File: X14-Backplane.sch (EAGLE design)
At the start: 28 parts, among them J2 PXC-PTSM-04-RA-1778641, J3 PXC-8-RA-1778683, J7 POE_TERMINAL

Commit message: X14-Backplane 11/29
This is the most up to date backplane as of 11/29/2021
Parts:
- removed C5: 47uF, Panasonic 47 uF cap - EEE-1CA470SP:47UF-POLAR-PANASONIC_D-35V-20%
- removed J7: POE_TERMINAL, Dist_POE:POE_TERMINAL
- added J8: PXC-8-RA-1778683, Phoenix Contact PTSM 8 pin:PXC-8-RA-1778683
- added U$9: IPL_13X2, PI-SHIELD, Solenoid-Backplane:IPL_13X2
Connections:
- new net +3V3: U$9.26
- new net ALERT1: U$9.16
- new net ALERT2: U$9.18
- new net SOL1_1: J8.8, U$9.5
- new net SOL2_1: J8.7, U$9.7
- new net SOL3_1: J8.6, U$9.9
- new net SOL4_1: J8.5, U$9.11
- new net SOL5_1: J8.4, U$9.13
- new net SOL6_1: J8.3, U$9.15
- new net SWCLK: U$9.10
- new net SWDIO: U$9.12
- net 12V: now also J8.1, J8.2, U$4.12V, U$9.25; no longer C5.+
- net 5V: now also U$9.2; no longer J7.1
- net C2_1: now also U$9.20
- net C2_2: now also U$9.19
- net CAN_H: now also U$9.21
- net CAN_L: now also U$9.23
- net CLK: now also U$9.22
- net DATA: now also U$9.24
- net GND: now also U$9.1, U$9.14, U$9.17, U$9.3, U$9.4, U$9.6, U$9.8; no longer C5.-, J7.2
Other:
- note added: "CAN io"
- note added: "PI Shield Connector"
- note added: "Power to ESC adapters"
- note added: "Reset Diode"
- note added: "Solenoid"
- note removed: "Prob dont need - note to ask grant"

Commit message: X14-Backplane 12/2
Most up to date backplane as of 12/2/2021
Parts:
- U$9: value IPL_13X2 -> 6X_CONN; device PI-SHIELD, Solenoid-Backplane:IPL_13X2 -> PI-SHIELD, Solenoid-Backplane:6X_CONN
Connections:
- removed net +3V3: U$9.26
- removed net ALERT1: U$9.16
- removed net ALERT2: U$9.18
- removed net GND: C4.2, J2.1, J3.1, J6.4, MUX.GND, MUX.GND2, MUX.INH, R1.1, R4.1, R5.1, U$1.10, U$2.10, U$3.10, U$4.GND_5V, U$8.P$1, U$9.1, U$9.14, U$9.17, U$9.3, U$9.4, U$9.6, U$9.8
- removed net SWCLK: U$9.10
- removed net SWDIO: U$9.12
- new net 12V_L: J8.1, J8.2, U$4.12V, U$9.14, U$9.16
- new net GND_L: C4.2, J2.1, J3.1, J6.4, MUX.GND, MUX.GND2, MUX.INH, R1.1, R4.1, R5.1, U$1.10, U$2.10, U$3.10, U$4.GND_12V, U$8.P$1, U$9.18, U$9.22
- new net JH: U$4.GND_5V
- net 12V: no longer J8.1, J8.2, U$4.12V, U$9.25
- net 3V3: now also U$9.24
- net 5V: now also U$9.20; no longer U$9.2
- net C2_1: no longer U$9.20
- net C2_2: no longer U$9.19
- net CAN_H: no longer U$9.21
- net CAN_L: no longer U$9.23
- net CLK: no longer U$9.22
- net DATA: no longer U$9.24
- net SOL1_1: now also J8.3, U$9.13; no longer J8.8, U$9.5
- net SOL2_1: now also J8.4, U$9.15; no longer J8.7, U$9.7
- net SOL3_1: now also J8.5, U$9.17; no longer J8.6, U$9.9
- net SOL4_1: now also J8.6, U$9.19; no longer J8.5, U$9.11
- net SOL5_1: now also J8.7, U$9.21; no longer J8.4, U$9.13
- net SOL6_1: now also J8.8, U$9.23; no longer J8.3, U$9.15

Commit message: X14-Backplane 12/4
This is the most up to date version as of 12/4/2021
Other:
- moved on the sheet: C4, J2, J6, R7, R8

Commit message: routing
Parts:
- removed J6: (no value), te 3.5m mm horiz 4 pin:284512-4
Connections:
- net 5V: no longer J6.1
- net CAN_H: no longer J6.2
- net CAN_L: no longer J6.3
- net GND_L: no longer J6.4
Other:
- note removed: "CAN to Logic"
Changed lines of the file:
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@@
 <part name="R5" library="SparkFun-Resistors" library_urn="urn:adsk.eagle:library:532" deviceset="1KOHM" device="-0603-1/10W-1%" package3d_urn="urn:adsk.eagle:package:39650/1" value="4.7k"/>
 <part name="DIST_TO_BACKPLANE" library="Samtec MPPT Hermaphoditic 10 pos - MPPT-10-01-01-L-RA-SD" deviceset="MPPT-10-01-01-L-RA-SD" device="" package3d_urn="urn:adsk.eagle:package:25115828/2"/>
-<part name="J6" library="te 3.5m mm horiz 4 pin" deviceset="284512-4" device="" package3d_urn="urn:adsk.eagle:package:24291286/2"/>
 <part name="H1" library="Mounting Holes" deviceset="6-32-HOLE" device="" package3d_urn="urn:adsk.eagle:package:24384748/2"/>
 <part name="H2" library="Mounting Holes" deviceset="6-32-HOLE" device="" package3d_urn="urn:adsk.eagle:package:24384748/2"/>
@@
 <sheet>
 <plain>
-<text x="149.86" y="-46.99" size="1.778" layer="91">CAN to Logic</text>
 <text x="149.86" y="-24.13" size="1.778" layer="91">CAN Debug</text>
 <text x="86.36" y="99.06" size="1.778" layer="91">Programmer</text>
@@
 <attribute name="NAME" x="39.37" y="55.372" size="1.778" layer="95" font="vector" rot="R180"/>
 </instance>
-<instance part="J6" gate="G$1" x="165.1" y="-57.15" smashed="yes">
-<attribute name="NAME" x="159.52" y="-49.53" size="1.778" layer="95"/>
-<attribute name="VALUE" x="160.02" y="-64.77" size="1.778" layer="96"/>
-</instance>
 <instance part="H1" gate="G$1" x="7.62" y="7.62" smashed="yes">
 <attribute name="NAME" x="7.62" y="10.16" size="1.016" layer="95" align="bottom-center"/>
@@
 </segment>
 <segment>
-<wire x1="157.48" y1="-54.61" x2="142.24" y2="-54.61" width="0.1524" layer="91"/>
-<label x="142.24" y="-54.61" size="1.778" layer="95"/>
-<pinref part="J6" gate="G$1" pin="2"/>
-</segment>
-<segment>
 <pinref part="R7" gate="&gt;NAME" pin="2"/>
 <wire x1="196.85" y1="-29.21" x2="196.85" y2="-26.67" width="0.1524" layer="91"/>
@@
 </segment>
 <segment>
-<wire x1="157.48" y1="-57.15" x2="142.24" y2="-57.15" width="0.1524" layer="91"/>
-<label x="142.24" y="-57.15" size="1.778" layer="95"/>
-<pinref part="J6" gate="G$1" pin="3"/>
-</segment>
-<segment>
 <pinref part="R8" gate="&gt;NAME" pin="1"/>
 <wire x1="196.85" y1="-54.61" x2="196.85" y2="-57.15" width="0.1524" layer="91"/>
@@
 </net>
 <net name="5V" class="0">
-<segment>
-<wire x1="157.48" y1="-52.07" x2="142.24" y2="-52.07" width="0.1524" layer="91"/>
-<pinref part="J6" gate="G$1" pin="1"/>
-<label x="142.24" y="-52.07" size="1.778" layer="95"/>
-</segment>
 <segment>
 <pinref part="U$4" gate="G$1" pin="5V"/>
@@
 </segment>
 <segment>
-<wire x1="157.48" y1="-59.69" x2="142.24" y2="-59.69" width="0.1524" layer="91"/>
-<pinref part="J6" gate="G$1" pin="4"/>
-<label x="142.24" y="-59.69" size="1.778" layer="95"/>
-</segment>
-<segment>

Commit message: rerouted board
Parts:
- U$9: value 6X_CONN -> 7X_CONN; device PI-SHIELD, Solenoid-Backplane:6X_CONN -> PI-SHIELD, Solenoid-Backplane:7X_CONN
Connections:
- removed net JH: U$4.GND_5V
- new net 12L_GND: U$4.GND_12V, U$9.18
- net CAN_H: now also U$9.2
- net CAN_L: now also U$9.1
- net GND_L: now also U$4.GND_5V; no longer U$4.GND_12V, U$9.18
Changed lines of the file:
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@@
 <?xml version="1.0" encoding="utf-8"?>
 <!DOCTYPE eagle SYSTEM "eagle.dtd">
-<eagle version="9.6.2">
+<eagle version="9.5.0">
 <drawing>
 <settings>
@@
 <part name="U$4" library="CONN, Distribution-Backplane" deviceset="BACKPLANE-DISTRIBUTION" device=""/>
 <part name="J8" library="Phoenix Contact PTSM 8 pin" deviceset="PXC-8-RA-1778683" device="" package3d_urn="urn:adsk.eagle:package:25224885/2"/>
-<part name="U$9" library="PI-SHIELD, Solenoid-Backplane" deviceset="6X_CONN" device=""/>
+<part name="U$9" library="PI-SHIELD, Solenoid-Backplane" deviceset="7X_CONN" device=""/>
 </parts>
 <sheets>
@@
 </segment>
 </net>
-<net name="JH" class="0">
-<segment>
-<pinref part="U$4" gate="G$1" pin="GND_5V"/>
-<wire x1="62.96" y1="31.62" x2="57.16" y2="31.62" width="0.1524" layer="91"/>
-<label x="55.1" y="32.03" size="1.778" layer="95"/>
-</segment>
-</net>
 <net name="SWDIO_3" class="0">
 <segment>
@@
 <label x="208.28" y="-26.67" size="1.778" layer="95"/>
 </segment>
+<segment>
+<pinref part="U$9" gate="G$1" pin="2"/>
+<wire x1="76.2" y1="-48.26" x2="67.31" y2="-48.26" width="0.1524" layer="91"/>
+<label x="67.31" y="-48.26" size="1.778" layer="95"/>
+</segment>
 </net>
 <net name="CAN_L" class="0">
@@
 <wire x1="196.85" y1="-57.15" x2="212.09" y2="-57.15" width="0.1524" layer="91"/>
 <label x="208.28" y="-57.15" size="1.778" layer="95"/>
+</segment>
+<segment>
+<pinref part="U$9" gate="G$1" pin="1"/>
+<wire x1="91.44" y1="-48.26" x2="100.33" y2="-48.26" width="0.1524" layer="91"/>
+<label x="92.71" y="-48.26" size="1.778" layer="95"/>
 </segment>
 </net>
@@
 <net name="GND_L" class="0">
 <segment>
-<pinref part="U$4" gate="G$1" pin="GND_12V"/>
-<wire x1="95.98" y1="26.54" x2="110.49" y2="26.54" width="0.1524" layer="91"/>
-<label x="102.108" y="26.67" size="1.778" layer="95"/>
-</segment>
-<segment>
 <pinref part="MUX" gate="G$1" pin="GND"/>
 <wire x1="22.86" y1="82.55" x2="17.78" y2="82.55" width="0.1524" layer="91"/>
@@
 </segment>
 <segment>
+<wire x1="100.33" y1="-43.18" x2="91.44" y2="-43.18" width="0.1524" layer="91"/>
+<pinref part="U$9" gate="G$1" pin="22"/>
+<label x="100.076" y="-41.148" size="1.778" layer="95" rot="R180"/>
+</segment>
+<segment>
+<pinref part="U$4" gate="G$1" pin="GND_5V"/>
+<wire x1="62.96" y1="31.62" x2="57.16" y2="31.62" width="0.1524" layer="91"/>
+<label x="52.56" y="32.03" size="1.778" layer="95"/>
+</segment>
+</net>
+<net name="12L_GND" class="0">
+<segment>
 <wire x1="100.33" y1="-38.1" x2="91.44" y2="-38.1" width="0.1524" layer="91"/>
 <pinref part="U$9" gate="G$1" pin="18"/>
@@
 </segment>
 <segment>
-<wire x1="100.33" y1="-43.18" x2="91.44" y2="-43.18" width="0.1524" layer="91"/>
-<pinref part="U$9" gate="G$1" pin="22"/>
-<label x="100.076" y="-41.148" size="1.778" layer="95" rot="R180"/>
-</segment>
-</net>
+<pinref part="U$4" gate="G$1" pin="GND_12V"/>
+<wire x1="95.98" y1="26.54" x2="109.22" y2="26.54" width="0.1524" layer="91"/>
+<wire x1="109.22" y1="26.54" x2="109.22" y2="26.67" width="0.1524" layer="91"/>
+<label x="104.14" y="26.67" size="1.778" layer="95"/>
+</segment>
+</net>

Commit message: afawevvew
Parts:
- added U$10: BACKPLANE->DATACONV, CONN, DataConversion-Backplane Connector- SAMTEC CLT-107-01-F-D:BACKPLANE->DATACONV
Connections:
- new net +3V3: U$10.1
- new net ALERT1: U$10.14
- new net ALERT2: U$10.12
- new net GND: U$10.2, U$10.3
- new net SWCLK: U$10.8
- new net SWDIO: U$10.6
- net C2_1: now also U$10.9
- net C2_2: now also U$10.7
- net CAN_H: now also U$10.10
- net CAN_L: now also U$10.11
- net CLK: now also U$10.5
- net DATA: now also U$10.4
- net NRST: now also U$10.13
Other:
- note added: "DataConversion Connector"
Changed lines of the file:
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@@
 <?xml version="1.0" encoding="utf-8"?>
 <!DOCTYPE eagle SYSTEM "eagle.dtd">
-<eagle version="9.5.0">
+<eagle version="9.6.2">
 <drawing>
 <settings>
@@
 <part name="J8" library="Phoenix Contact PTSM 8 pin" deviceset="PXC-8-RA-1778683" device="" package3d_urn="urn:adsk.eagle:package:25224885/2"/>
 <part name="U$9" library="PI-SHIELD, Solenoid-Backplane" deviceset="7X_CONN" device=""/>
+<part name="U$10" library="CONN, DataConversion-Backplane Connector- SAMTEC CLT-107-01-F-D" deviceset="BACKPLANE-&gt;DATACONV" device=""/>
 </parts>
 <sheets>
@@
 <text x="72.67" y="-23.96" size="1.778" layer="91">PI Shield Connector</text>
 <text x="191.02" y="-19.88" size="1.778" layer="91">CAN io</text>
+<text x="34.57" y="-73.49" size="1.778" layer="91">DataConversion Connector</text>
 </plain>
 <instances>
@@
 </instance>
 <instance part="U$9" gate="G$1" x="83.82" y="-39.37" smashed="yes"/>
+<instance part="U$10" gate="G$1" x="38.1" y="-83.82" smashed="yes">
+<attribute name="NAME" x="38.1" y="-78.74" size="2.54" layer="95"/>
+</instance>
 </instances>
 <busses>
@@
 <label x="67.31" y="-48.26" size="1.778" layer="95"/>
 </segment>
+<segment>
+<wire x1="73.66" y1="-93.98" x2="63.5" y2="-93.98" width="0.1524" layer="91"/>
+<label x="68.58" y="-93.98" size="1.778" layer="95"/>
+<pinref part="U$10" gate="G$1" pin="10"/>
+</segment>
 </net>
 <net name="CAN_L" class="0">
@@
 <wire x1="91.44" y1="-48.26" x2="100.33" y2="-48.26" width="0.1524" layer="91"/>
 <label x="92.71" y="-48.26" size="1.778" layer="95"/>
+</segment>
+<segment>
+<wire x1="25.4" y1="-96.52" x2="33.02" y2="-96.52" width="0.1524" layer="91"/>
+<label x="22.86" y="-96.52" size="1.778" layer="95"/>
+<pinref part="U$10" gate="G$1" pin="11"/>
 </segment>
 </net>
@@
 <junction x="243.84" y="60.96"/>
 </segment>
+<segment>
+<wire x1="33.02" y1="-99.06" x2="25.4" y2="-99.06" width="0.1524" layer="91"/>
+<label x="22.86" y="-99.06" size="1.778" layer="95"/>
+<pinref part="U$10" gate="G$1" pin="13"/>
+</segment>
 </net>
 <net name="ESCID_1" class="0">
@@
 <label x="105" y="34.4" size="1.778" layer="95"/>
 </segment>
+<segment>
+<wire x1="33.02" y1="-88.9" x2="25.4" y2="-88.9" width="0.1524" layer="91"/>
+<label x="22.86" y="-88.9" size="1.778" layer="95"/>
+<pinref part="U$10" gate="G$1" pin="5"/>
+</segment>
 </net>
 <net name="C2_1" class="0">
@@
 <label x="104.1" y="31.8" size="1.778" layer="95"/>
 </segment>
+<segment>
+<wire x1="33.02" y1="-93.98" x2="25.4" y2="-93.98" width="0.1524" layer="91"/>
+<label x="22.86" y="-93.98" size="1.778" layer="95"/>
+<pinref part="U$10" gate="G$1" pin="9"/>
+</segment>
 </net>
 <net name="C2_2" class="0">
@@
 <label x="104.3" y="29.3" size="1.778" layer="95"/>
 </segment>
+<segment>
+<wire x1="25.4" y1="-91.44" x2="33.02" y2="-91.44" width="0.1524" layer="91"/>
+<label x="22.86" y="-91.44" size="1.778" layer="95"/>
+<pinref part="U$10" gate="G$1" pin="7"/>
+</segment>
 </net>
 <net name="DATA" class="0">
@@
 <wire x1="95.98" y1="41.78" x2="109.81" y2="41.78" width="0.1524" layer="91"/>
 <label x="103.2" y="42.1" size="1.778" layer="95"/>
+</segment>
+<segment>
+<wire x1="63.5" y1="-86.36" x2="73.66" y2="-86.36" width="0.1524" layer="91"/>
+<label x="68.58" y="-86.36" size="1.778" layer="95"/>
+<pinref part="U$10" gate="G$1" pin="4"/>
 </segment>
 </net>
@@
 </segment>
 </net>
+<net name="GND" class="0">
+<segment>
+<wire x1="33.02" y1="-86.36" x2="25.4" y2="-86.36" width="0.1524" layer="91"/>
+<label x="22.86" y="-86.36" size="1.778" layer="95"/>
+<pinref part="U$10" gate="G$1" pin="3"/>
+</segment>
+<segment>
+<wire x1="63.5" y1="-83.82" x2="73.66" y2="-83.82" width="0.1524" layer="91"/>
+<label x="68.58" y="-83.82" size="1.778" layer="95"/>
+<pinref part="U$10" gate="G$1" pin="2"/>
+</segment>
+</net>
+<net name="+3V3" class="0">
+<segment>
+<wire x1="33.02" y1="-83.82" x2="25.4" y2="-83.82" width="0.1524" layer="91"/>
+<label x="22.86" y="-83.82" size="1.778" layer="95"/>
+<pinref part="U$10" gate="G$1" pin="1"/>
+</segment>
+</net>
+<net name="SWDIO" class="0">
+<segment>
+<wire x1="63.5" y1="-88.9" x2="73.66" y2="-88.9" width="0.1524" layer="91"/>
+<label x="68.58" y="-88.9" size="1.778" layer="95"/>
+<pinref part="U$10" gate="G$1" pin="6"/>
+</segment>
+</net>
+<net name="SWCLK" class="0">
+<segment>
+<wire x1="63.5" y1="-91.44" x2="73.66" y2="-91.44" width="0.1524" layer="91"/>
+<label x="68.58" y="-91.44" size="1.778" layer="95"/>
+<pinref part="U$10" gate="G$1" pin="8"/>
+</segment>
+</net>
+<net name="ALERT2" class="0">
+<segment>
+<wire x1="73.66" y1="-96.52" x2="63.5" y2="-96.52" width="0.1524" layer="91"/>
+<label x="68.58" y="-96.52" size="1.778" layer="95"/>
+<pinref part="U$10" gate="G$1" pin="12"/>
+</segment>
+</net>
+<net name="ALERT1" class="0">
+<segment>
+<wire x1="63.5" y1="-99.06" x2="73.66" y2="-99.06" width="0.1524" layer="91"/>
+<label x="68.58" y="-99.06" size="1.778" layer="95"/>
+<pinref part="U$10" gate="G$1" pin="14"/>
+</segment>
+</net>

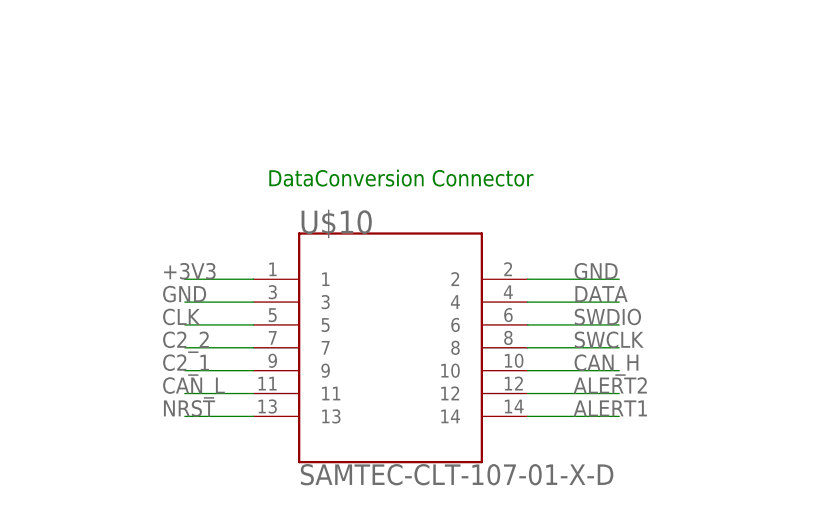
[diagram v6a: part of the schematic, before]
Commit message: Implemented conversion board
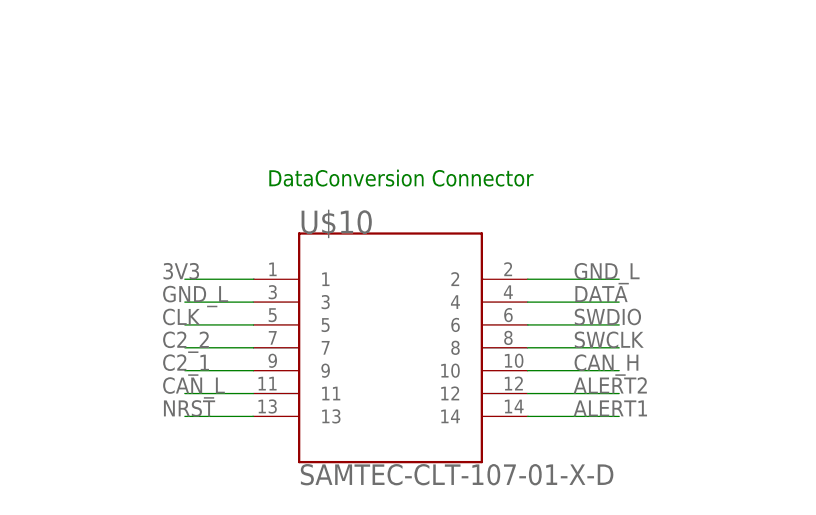
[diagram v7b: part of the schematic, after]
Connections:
- removed net +3V3: U$10.1
- removed net GND: U$10.2, U$10.3
- net 3V3: now also U$10.1
- net GND_L: now also U$10.2, U$10.3
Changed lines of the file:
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@@
 <label x="100.33" y="-43.688" size="1.778" layer="95" rot="R180"/>
+</segment>
+<segment>
+<wire x1="33.02" y1="-83.82" x2="25.4" y2="-83.82" width="0.1524" layer="91"/>
+<label x="22.86" y="-83.82" size="1.778" layer="95"/>
+<pinref part="U$10" gate="G$1" pin="1"/>
 </segment>
 </net>
@@
 <label x="52.56" y="32.03" size="1.778" layer="95"/>
 </segment>
+<segment>
+<wire x1="33.02" y1="-86.36" x2="25.4" y2="-86.36" width="0.1524" layer="91"/>
+<label x="22.86" y="-86.36" size="1.778" layer="95"/>
+<pinref part="U$10" gate="G$1" pin="3"/>
+</segment>
+<segment>
+<wire x1="63.5" y1="-83.82" x2="73.66" y2="-83.82" width="0.1524" layer="91"/>
+<label x="68.58" y="-83.82" size="1.778" layer="95"/>
+<pinref part="U$10" gate="G$1" pin="2"/>
+</segment>
 </net>
 <net name="12L_GND" class="0">
@@
 </segment>
 </net>
-<net name="GND" class="0">
-<segment>
-<wire x1="33.02" y1="-86.36" x2="25.4" y2="-86.36" width="0.1524" layer="91"/>
-<label x="22.86" y="-86.36" size="1.778" layer="95"/>
-<pinref part="U$10" gate="G$1" pin="3"/>
-</segment>
-<segment>
-<wire x1="63.5" y1="-83.82" x2="73.66" y2="-83.82" width="0.1524" layer="91"/>
-<label x="68.58" y="-83.82" size="1.778" layer="95"/>
-<pinref part="U$10" gate="G$1" pin="2"/>
-</segment>
-</net>
-<net name="+3V3" class="0">
-<segment>
-<wire x1="33.02" y1="-83.82" x2="25.4" y2="-83.82" width="0.1524" layer="91"/>
-<label x="22.86" y="-83.82" size="1.778" layer="95"/>
-<pinref part="U$10" gate="G$1" pin="1"/>
-</segment>
-</net>
